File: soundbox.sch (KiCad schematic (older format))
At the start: 185 parts, among them J10 COLOR INPUT, J11 MONO INPUT, J12 NEXT PWR INPUT 1, J13 NEXT PWR INPUT 2, J14 -12VDC OUT, J15 5VDC STANDBY, J16 MON IN 1, J17 MON IN 2, J18 PA1, J19 BOOT0, J2 OUT (SJ1-3535NG), J20 PC0, J21 PC1, J22 PB0, J23 PB1, J24 R SPK, J25 R SPEAKER (SJ-2509N), J26 L SPEAKER, J27 L SPK, J28 I2C Ext, J29 OLED, J3 MIC (SJ1-3535NG), J30 BOOT1, J31 NeXT Keyboard, J32 NeXT Keyboard (MD-50SM / KMDG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, J4 USB Host (SS-52100-001), J5 Mic IN, J6 Audio OUT, J7 STLINK, J8 UART2, J9 PA0, Q1 2SC2712, SW1 NeXT POWER SW (1-1825027-1 / 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, SW3 NeXT POWER SW, SW4 MCU RESET, U11 TLV70033DDCR, U17 USBLC6-2SC6, U18 STMPS2151STR‎ or TPS2051CDBV, U19 SN74LVC2G34DBV, U20 PCM5122PW, U21 TLV70033DDCR (or XC6204B332MR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, U22 TLV70033DDCR (or XC6204B332MR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, U23 PLT133/T, U24 STM32F401RCT6, U25 SN74LVC1G07DBV, U26 SN74HCT125DR, U27 TLV320ADC3100, U28 BD33FC0FP, U29 TPA2005D1DGN, U30 BD33FC0FP, U31 TPA2005D1DGN, U32 PCA9515AD, U8 5V(DC/DC), X3 ECS-2520MVLC-225.792-BN-TR, Y2 25MHz (FA-238 25.0000MB-K0)

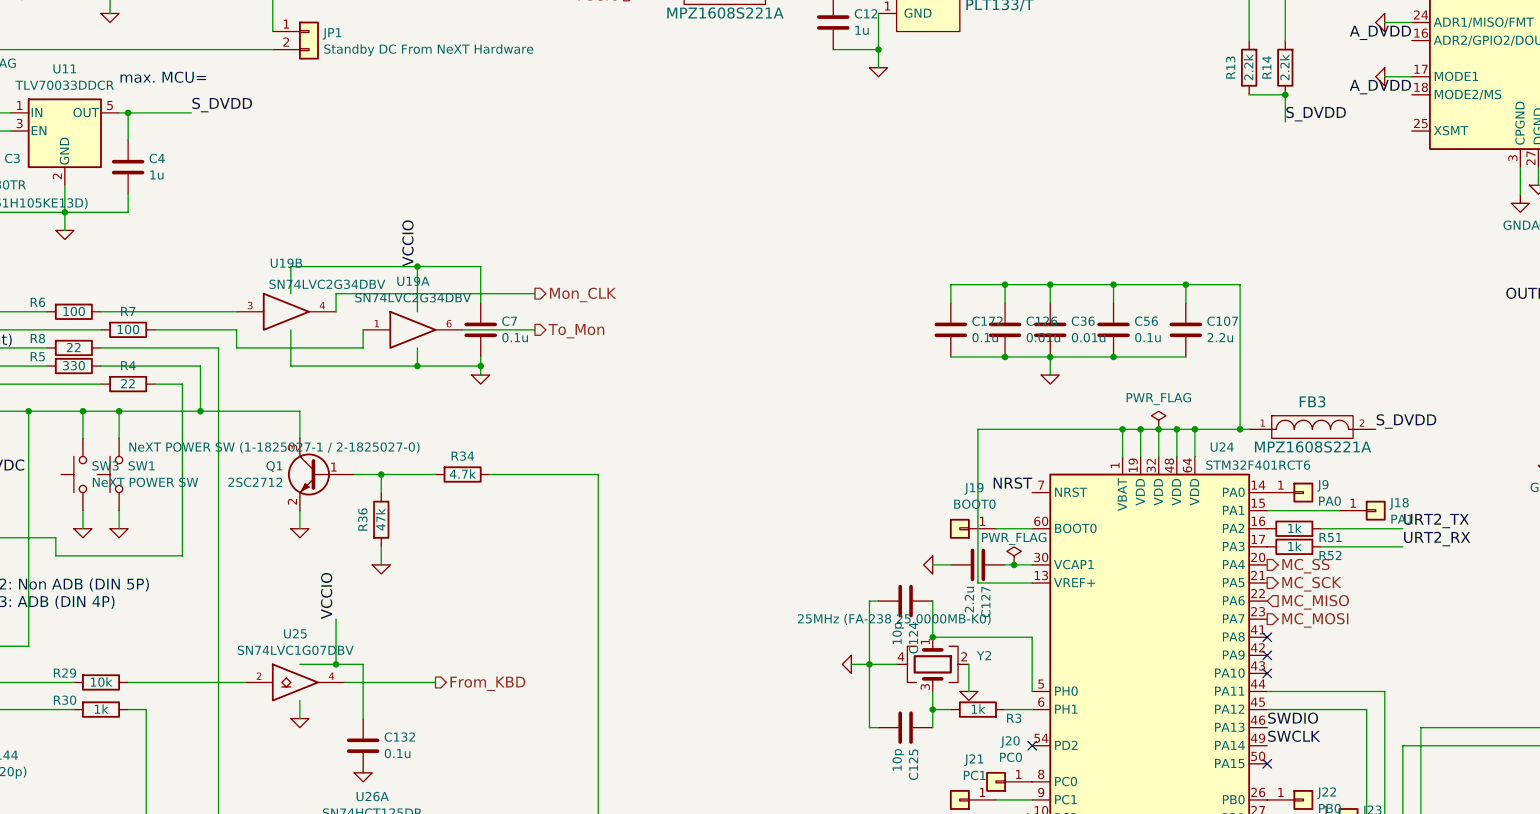
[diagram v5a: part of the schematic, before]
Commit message: connect XSMT (errata)
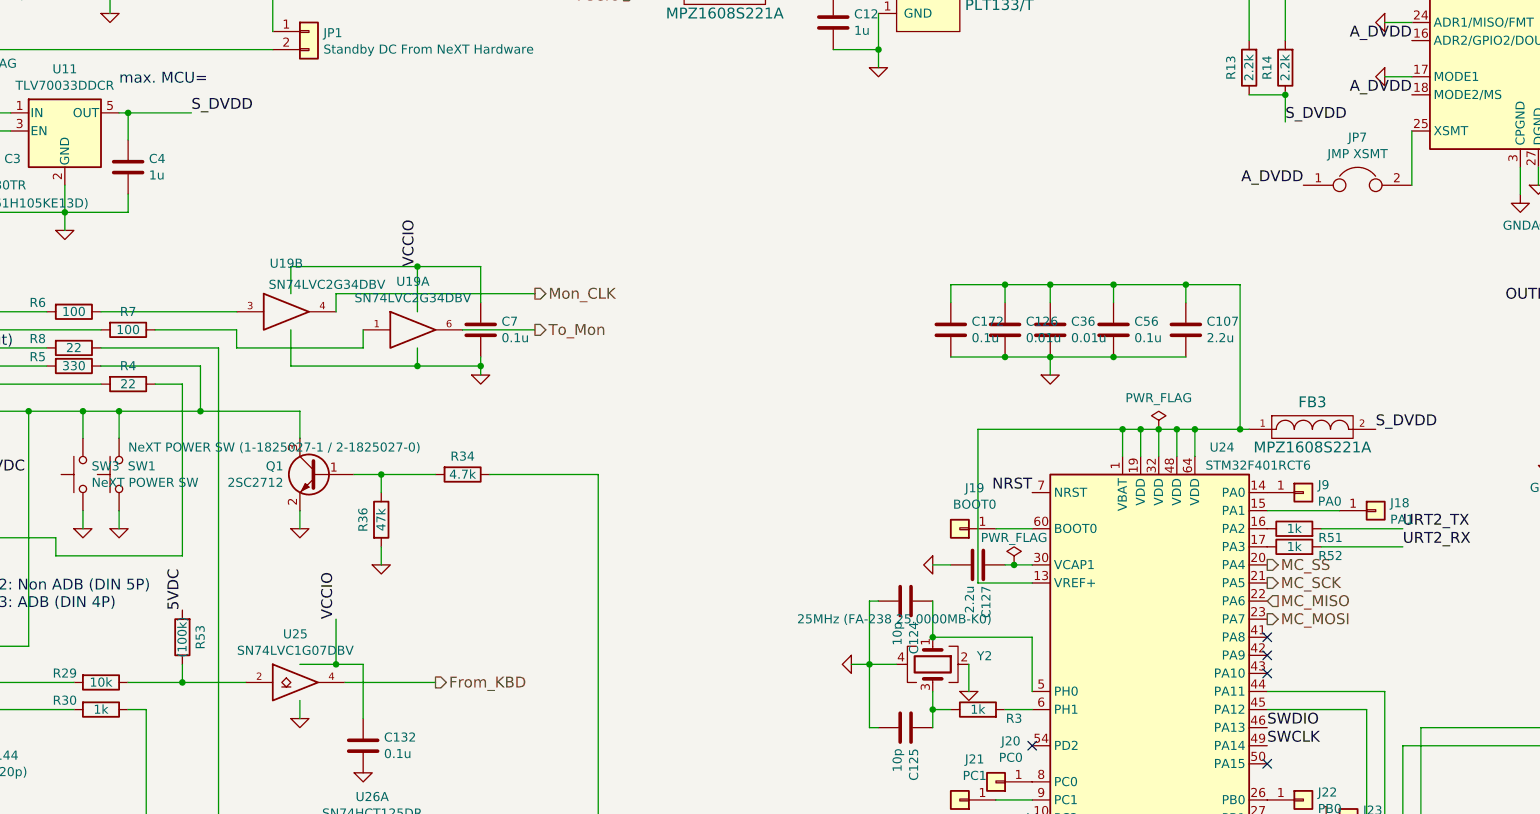
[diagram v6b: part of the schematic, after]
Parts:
- added JP7: JMP XSMT, Jumper:SolderJumper-2_P1.3mm_Bridged_RoundedPad1.0x1.5mm, symbol Device:Jumper
- added R53: (100k), Resistor_SMD:R_0603_1608Metric_Pad1.05x0.95mm_HandSolder, symbol Device:R
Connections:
- net 5VDC_OUT: now also R53.2
- net A_DVDD: now also JP7.1
- net at U20.25 (XSMT): now also JP7.2
- net at R29.1, U25.2: now also R53.1
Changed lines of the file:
@@
 $EndComp
 Wire Wire Line
-	4250 6100 4900 6100
+	4250 6100 4550 6100
 Wire Wire Line
 	5200 6000 5400 6000
@@
 Wire Wire Line
 	10900 6950 10900 7300
+$Comp
+L Device:R R53
+U 1 1 5F70D8AE
+P 4550 5850
+F 0 "R53" V 4450 5850 50  0000 C CNN
+F 1 "(100k)" V 4550 5850 50  0000 C CNN
+F 2 "Resistor_SMD:R_0603_1608Metric_Pad1.05x0.95mm_HandSolder" V 4480 5850 50  0001 C CNN
+F 3 "~" H 4550 5850 50  0001 C CNN
+	1    4550 5850
+	-1   0    0    1
+$EndComp
+Wire Wire Line
+	4550 6000 4550 6100
+Connection ~ 4550 6100
+Wire Wire Line
+	4550 6100 4900 6100
+Text Label 4550 5700 1    60   ~ 0
+5VDC
+$Comp
+L Device:Jumper JP7
+U 1 1 5F81B22E
+P 11050 3350
+F 0 "JP7" H 11050 3614 50  0000 C CNN
+F 1 "JMP XSMT" H 11050 3523 50  0000 C CNN
+F 2 "Jumper:SolderJumper-2_P1.3mm_Bridged_RoundedPad1.0x1.5mm" H 11050 3350 50  0001 C CNN
+F 3 "~" H 11050 3350 50  0001 C CNN
+	1    11050 3350
+	1    0    0    -1
+$EndComp
+Text Label 10750 3350 2    60   ~ 0
+A_DVDD
+Wire Wire Line
+	11350 3050 11350 3350
 $EndSCHEMATC

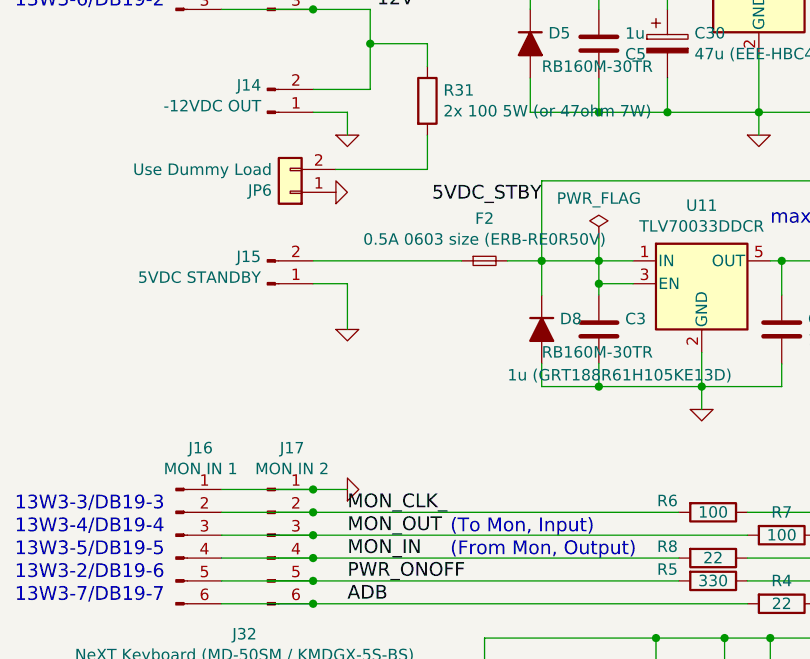
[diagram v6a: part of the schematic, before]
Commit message: add protection zener
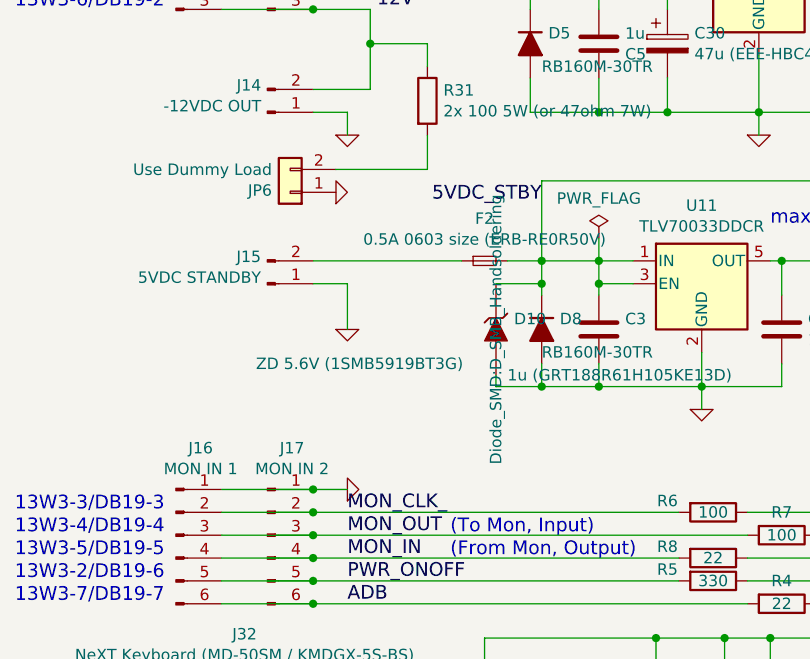
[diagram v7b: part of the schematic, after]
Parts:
- added D10: ZD 5.6V (1SMB5919BT3G), Diode_SMD:D_SMB_Handsoldering, symbol ossc_board-rescue:ZENER
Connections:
- net 5VDC_STBY: now also D10.1 (K)
- net GND: now also D10.2 (A)
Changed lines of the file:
@@
 	3450 3500 3900 3500
 Wire Wire Line
-	3200 2950 3200 3100
+	3200 2950 3200 3050
 Wire Wire Line
 	3600 3050 3450 3050
@@
 Wire Wire Line
 	11350 3050 11350 3350
+$Comp
+L ossc_board-rescue:ZENER D10
+U 1 1 5F8E9495
+P 3000 3250
+F 0 "D10" V 2954 3329 50  0000 L CNN
+F 1 "ZD 5.6V (1SMB5919BT3G)" V 3150 2200 50  0000 L CNN
+F 2 "Diode_SMD:D_SMB_Handsoldering" H 3000 3250 50  0000 C CNN
+F 3 "" H 3000 3250 50  0000 C CNN
+	1    3000 3250
+	0    1    1    0
+$EndComp
+Wire Wire Line
+	3000 3050 3200 3050
+Connection ~ 3200 3050
+Wire Wire Line
+	3200 3050 3200 3100
+Wire Wire Line
+	3200 3500 3000 3500
+Wire Wire Line
+	3000 3500 3000 3450
+Connection ~ 3200 3500
 $EndSCHEMATC

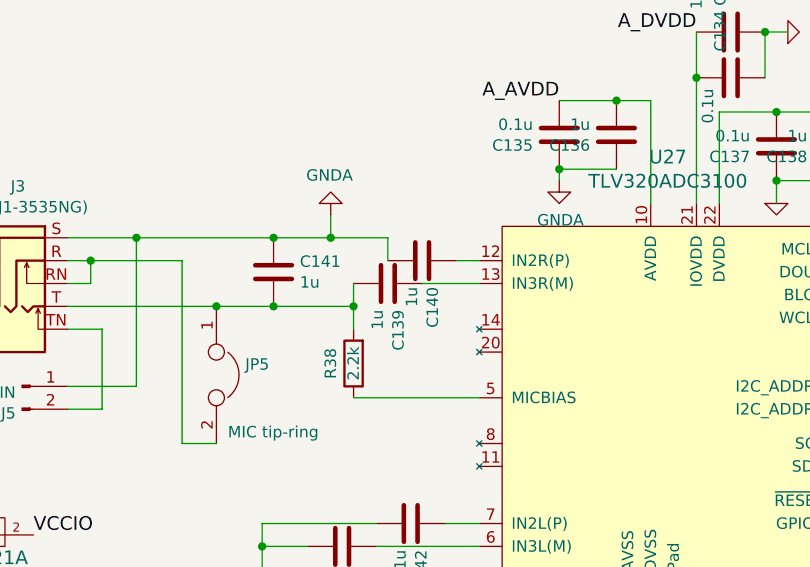
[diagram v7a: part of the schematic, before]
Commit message: update mic lines
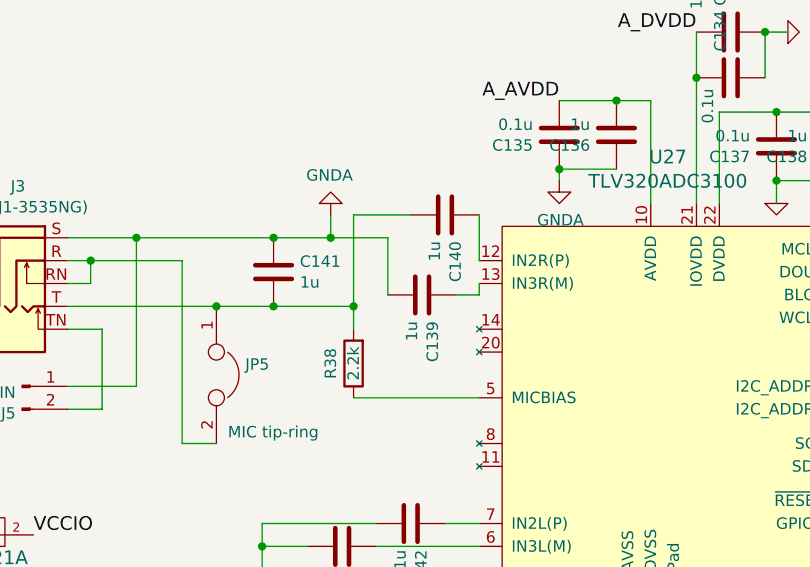
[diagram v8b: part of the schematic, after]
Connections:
- net GNDA: now also C139.2; no longer C140.2
- net at C141.2, J3.T, JP5.1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: now also C140.2; no longer C139.2
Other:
- moved on the sheet: C139, C140
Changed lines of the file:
@@
 VCCIO
-Wire Wire Line
-	6050 9200 5950 9200
 Wire Wire Line
 	5600 10450 6050 10450
@@
 Wire Wire Line
 	5400 9100 5150 9100
-Connection ~ 5400 9100
 Wire Wire Line
 	5400 9000 5400 9100
@@
 $EndComp
 Wire Wire Line
-	5650 9100 5400 9100
-Wire Wire Line
-	5650 9200 5650 9100
-Wire Wire Line
 	5500 9400 5150 9400
-Wire Wire Line
-	5500 9300 5500 9400
-Wire Wire Line
-	6050 9300 5800 9300
 $Comp
 L Device:C C141
@@
 L Device:C C140
 U 1 1 6138C042
-P 5800 9200
-F 0 "C140" H 5915 9246 50  0000 L CNN
-F 1 "1u" H 5915 9155 50  0000 L CNN
-F 2 "Capacitor_SMD:C_0603_1608Metric_Pad1.05x0.95mm_HandSolder" H 5838 9050 50  0001 C CNN
-F 3 "~" H 5800 9200 50  0001 C CNN
-	1    5800 9200
+P 5900 9000
+F 0 "C140" H 6015 9046 50  0000 L CNN
+F 1 "1u" H 6015 8955 50  0000 L CNN
+F 2 "Capacitor_SMD:C_0603_1608Metric_Pad1.05x0.95mm_HandSolder" H 5938 8850 50  0001 C CNN
+F 3 "~" H 5900 9000 50  0001 C CNN
+	1    5900 9000
 	0    1    1    0
 $EndComp
@@
 L Device:C C139
 U 1 1 6138C6B3
-P 5650 9300
-F 0 "C139" H 5765 9346 50  0000 L CNN
-F 1 "1u" H 5765 9255 50  0000 L CNN
-F 2 "Capacitor_SMD:C_0603_1608Metric_Pad1.05x0.95mm_HandSolder" H 5688 9150 50  0001 C CNN
-F 3 "~" H 5650 9300 50  0001 C CNN
-	1    5650 9300
+P 5800 9350
+F 0 "C139" H 5915 9396 50  0000 L CNN
+F 1 "1u" H 5915 9305 50  0000 L CNN
+F 2 "Capacitor_SMD:C_0603_1608Metric_Pad1.05x0.95mm_HandSolder" H 5838 9200 50  0001 C CNN
+F 3 "~" H 5800 9350 50  0001 C CNN
+	1    5800 9350
 	0    1    1    0
 $EndComp
@@
 	3000 3500 3000 3450
 Connection ~ 3200 3500
+Wire Wire Line
+	5400 9100 5650 9100
+Wire Wire Line
+	5650 9100 5650 9350
+Connection ~ 5400 9100
+Wire Wire Line
+	6050 9300 6050 9350
+Wire Wire Line
+	6050 9350 5950 9350
+Wire Wire Line
+	6050 9200 6050 9000
+Wire Wire Line
+	5750 9000 5500 9000
+Wire Wire Line
+	5500 9000 5500 9400
 $EndSCHEMATC
